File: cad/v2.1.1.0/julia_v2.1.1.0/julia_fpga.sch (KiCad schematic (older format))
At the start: 26 parts, among them U1 EP4CE6F17, X1 50MHz

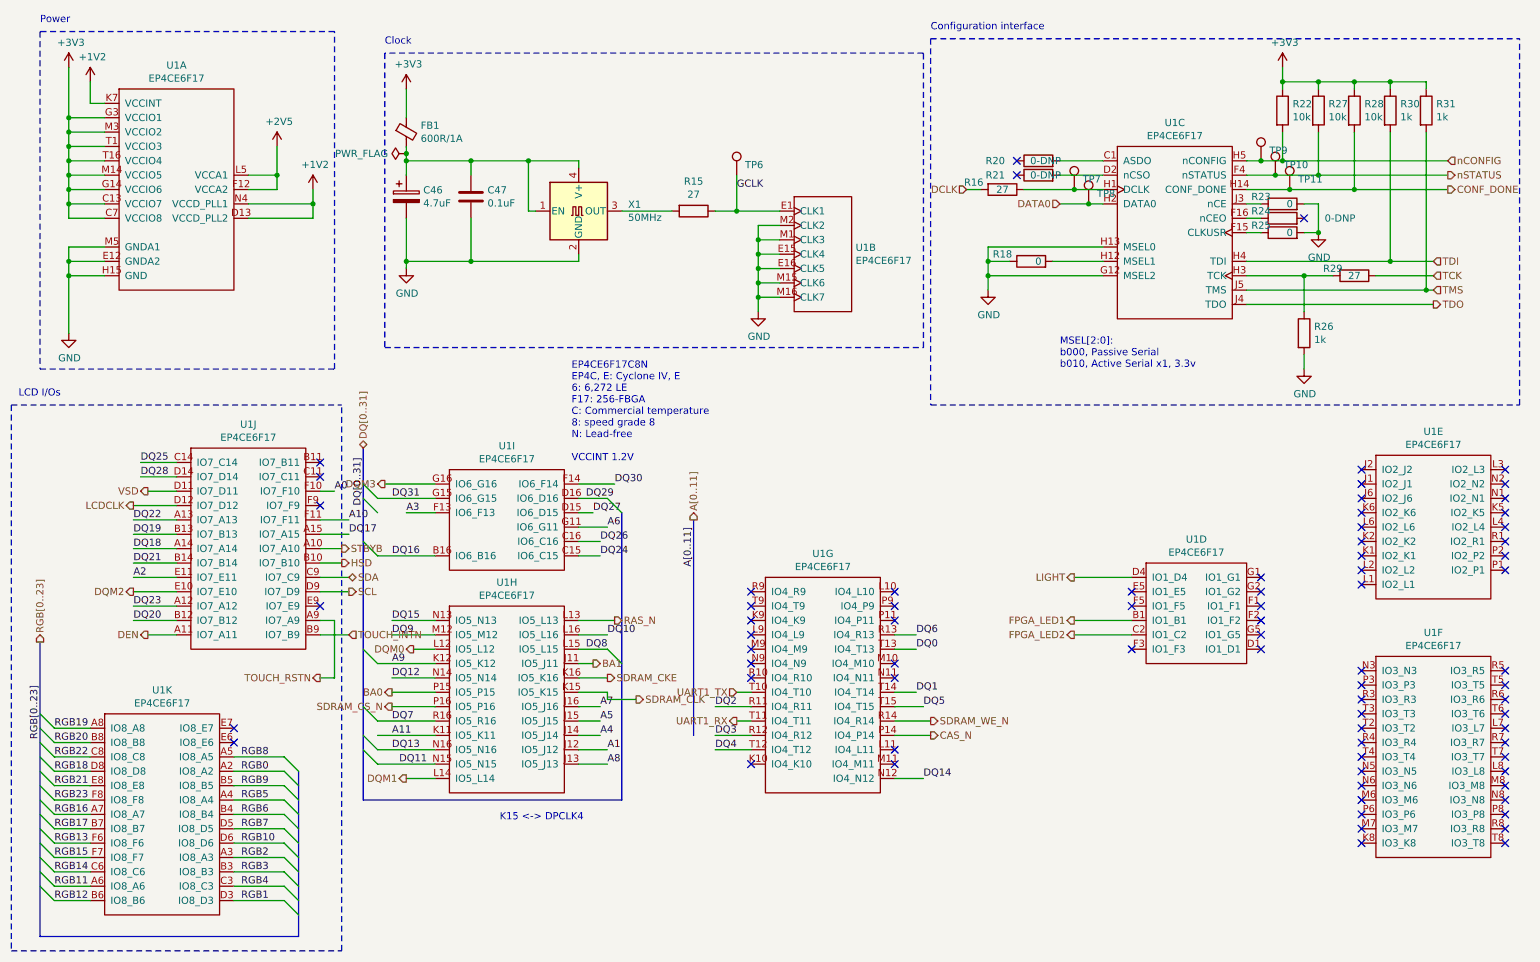
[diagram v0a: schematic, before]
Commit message: Clean up v2.1.1.0 FPGA sheet; update BOM
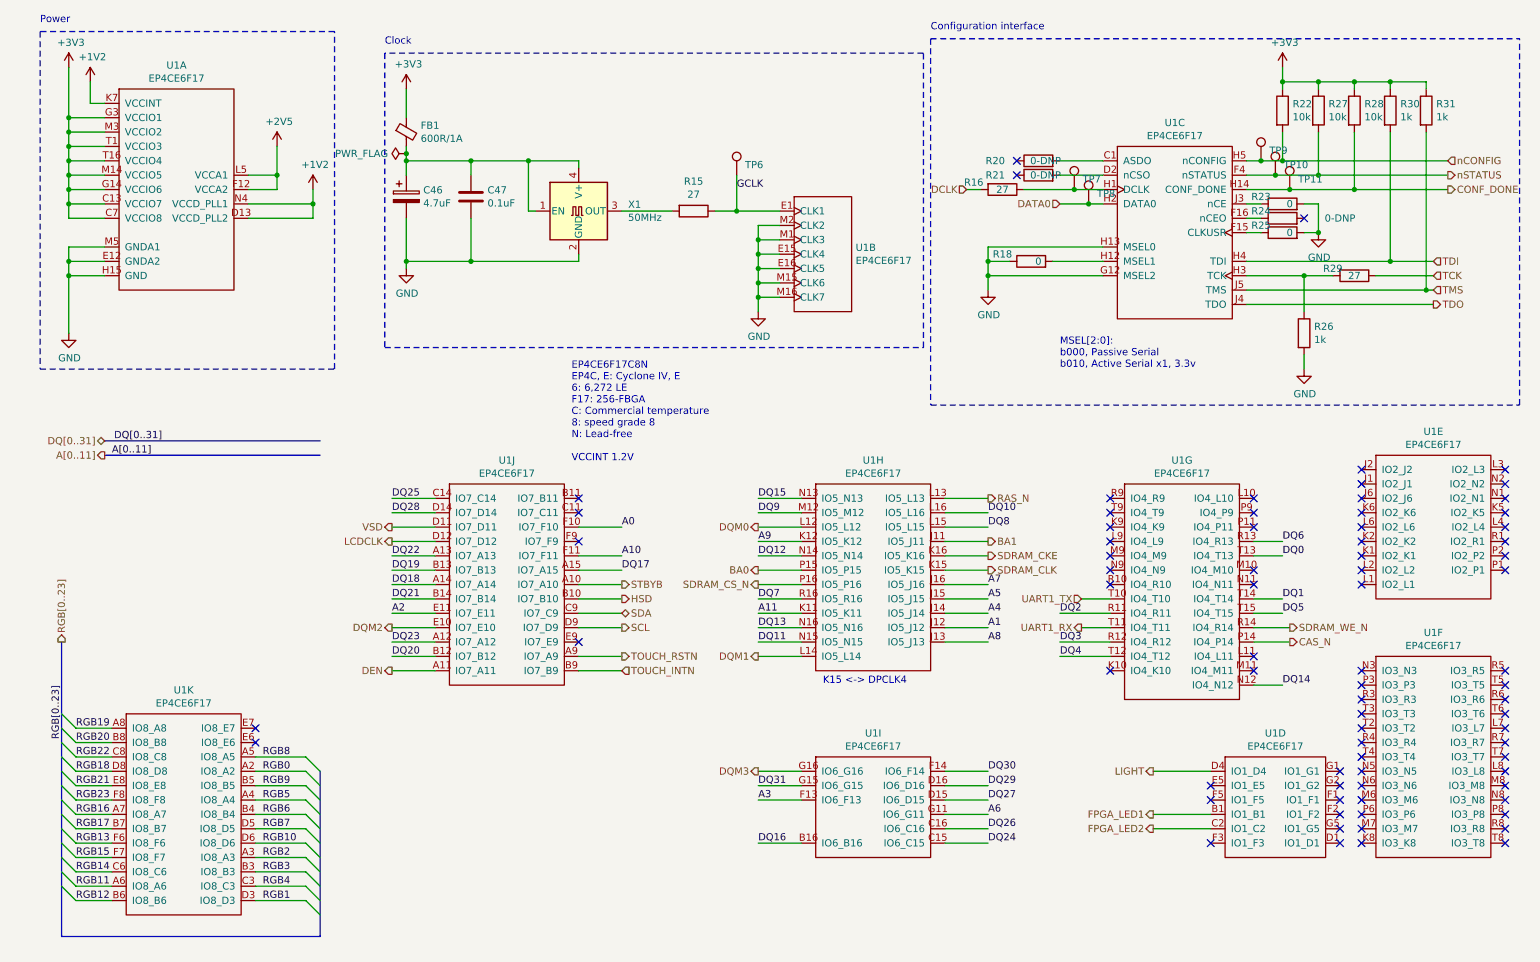
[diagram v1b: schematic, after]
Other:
- note removed: "LCD I/Os"
- moved on the sheet: U1D, U1G, U1H, U1I, U1J, U1K

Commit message: Updated 3d rendering
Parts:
- X1: footprint Oscillator:Oscillator_SMD_EuroQuartz_XO91-4Pin_7.0x5.0mm -> ik:Oscillator_SMD_EuroQuartz_XO91-4Pin_7.0x5.0mm
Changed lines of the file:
@@
 F 0 "X1" H 4944 1896 50  0000 L CNN
 F 1 "50MHz" H 4944 1805 50  0000 L CNN
-F 2 "Oscillator:Oscillator_SMD_EuroQuartz_XO91-4Pin_7.0x5.0mm" H 5300 1500 50  0001 C CNN
+F 2 "ik:Oscillator_SMD_EuroQuartz_XO91-4Pin_7.0x5.0mm" H 5300 1500 50  0001 C CNN
 F 3 "http://cdn-reichelt.de/documents/datenblatt/B400/XO91.pdf" H 4500 1850 50  0001 C CNN
 	1    4600 1850
